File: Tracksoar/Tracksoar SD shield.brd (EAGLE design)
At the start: 44 x 19.5 mm, 8 parts, among them U1 HEX_CONVERTER

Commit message: removed old shields
removed square shields and added values to shield passives
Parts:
- C1: value (none) -> 10uf
- C2: value (none) -> .1uf
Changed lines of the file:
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@@
 <attribute name="PROD_ID" value="IC-09604" x="24.511" y="8.89" size="1.778" layer="28" rot="MR270" display="off"/>
 </element>
-<element name="C1" library="SparkFun-Passives" package="0805" value="" x="26.2636" y="16.891" rot="MR180"/>
-<element name="C2" library="SparkFun-Passives" package="0805" value="" x="26.2382" y="15.1638" rot="MR180"/>
+<element name="C1" library="SparkFun-Passives" package="0805" value="10uf" x="26.2636" y="16.891" rot="MR180"/>
+<element name="C2" library="SparkFun-Passives" package="0805" value=".1uf" x="26.2382" y="15.1638" rot="MR180"/>
 </elements>
 <signals>

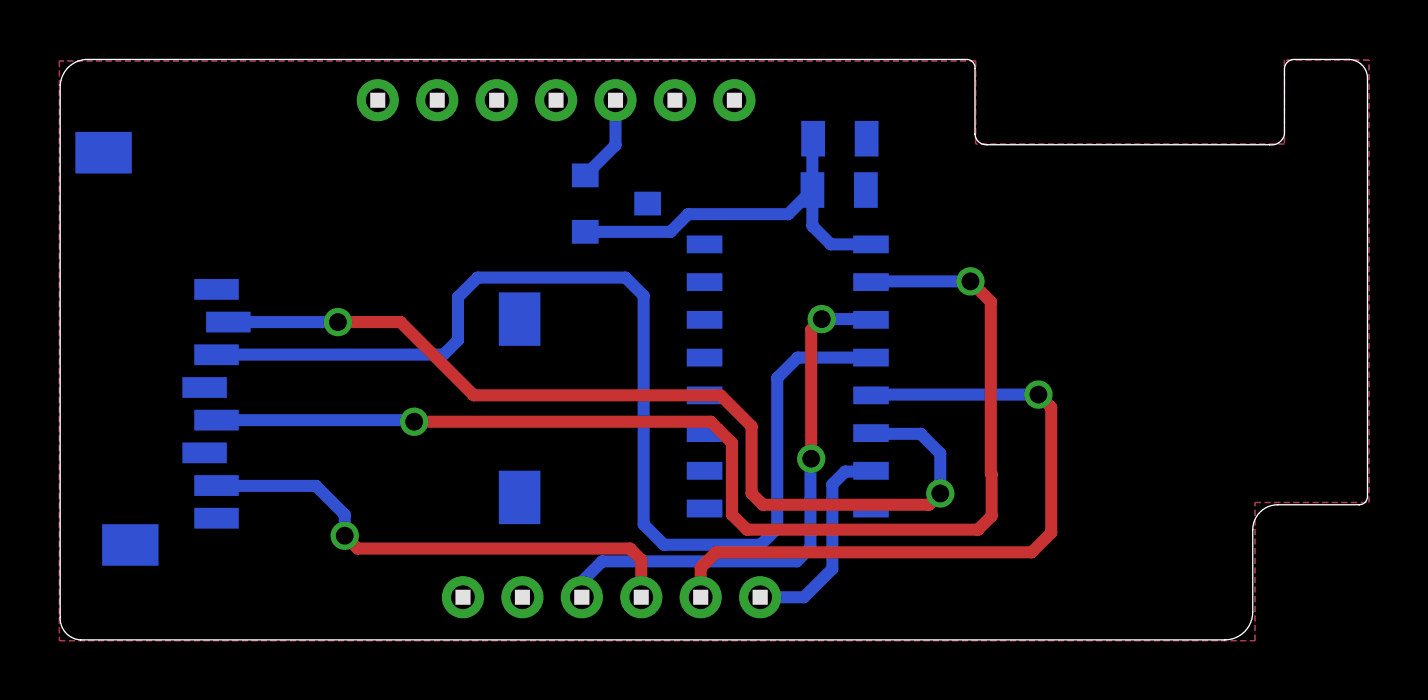
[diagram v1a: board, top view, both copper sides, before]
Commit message: Fixed shield board length
fixed the shield length to not interfere with power and radio
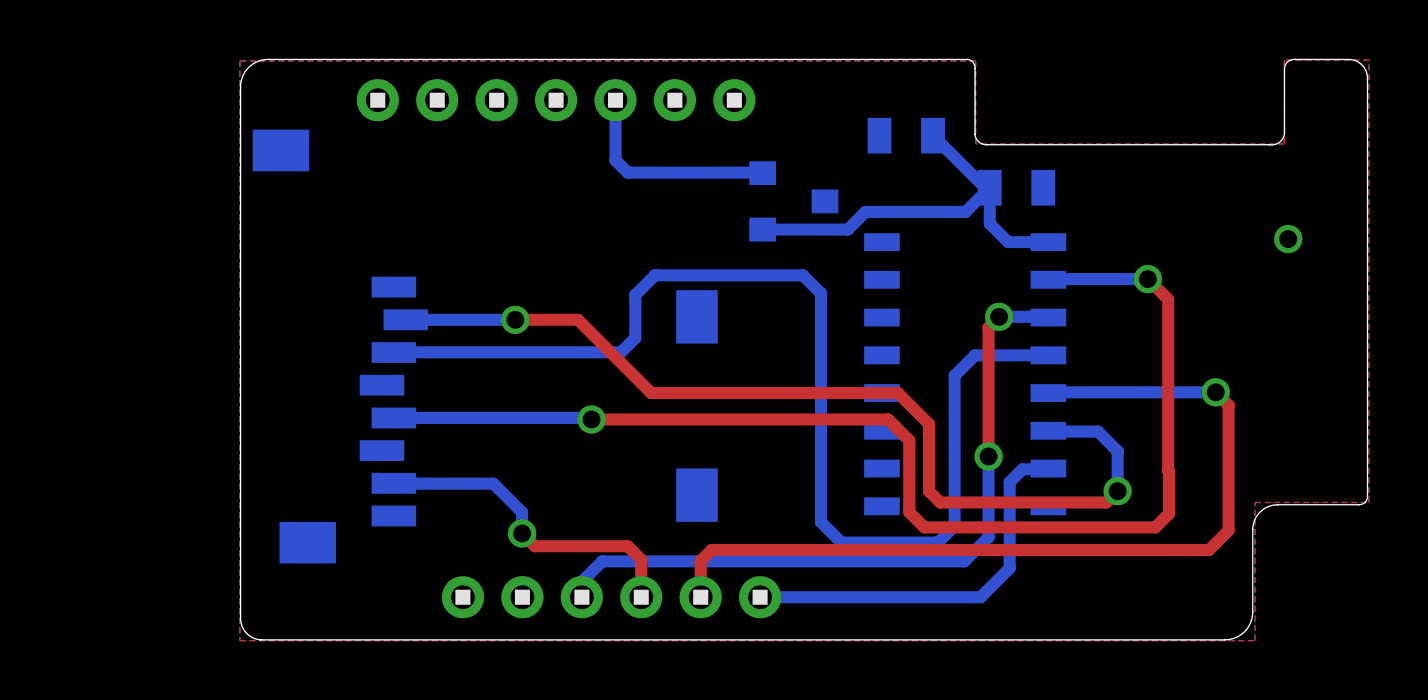
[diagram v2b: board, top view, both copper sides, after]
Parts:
- moved C2 5.97 mm to (32.2, 15.2)
- moved U1 5.97 mm to (30.5, 8.97)
- moved U$1 5.97 mm to (21.9, 2.90)
- moved U$2 5.97 mm to (24.7, 14.8)
- moved C1 2.24 mm to (28.5, 17.0), turned to 0 degrees
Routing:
- net MOSI: track 23.7 -> 29.9 mm
- net SS: track 7.16 -> 13.2 mm
- net MISO: track 17.0 -> 11.1 mm
- net SCK: track 18.2 -> 24.1 mm
- net VCC: track 2.95 -> 7.15 mm
- net 3V: track 13.4 -> 14.3 mm
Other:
- board size 44 x 19.5 mm -> 37.9 x 19.5 mm

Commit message: replaced sd with eeprom
the atmega328p does not have enough SRAM to handle the Trackuino duties
and SD read / write. It has been replace with an ST Micro M24M02 2Mb
eeprom. This will result in much less RAM usage, a smaller BOM, lower
cost, and lower power usage. However it also means we lose portability
of storage and easy computer interfacing. We’ll look at revising this
in future versions.
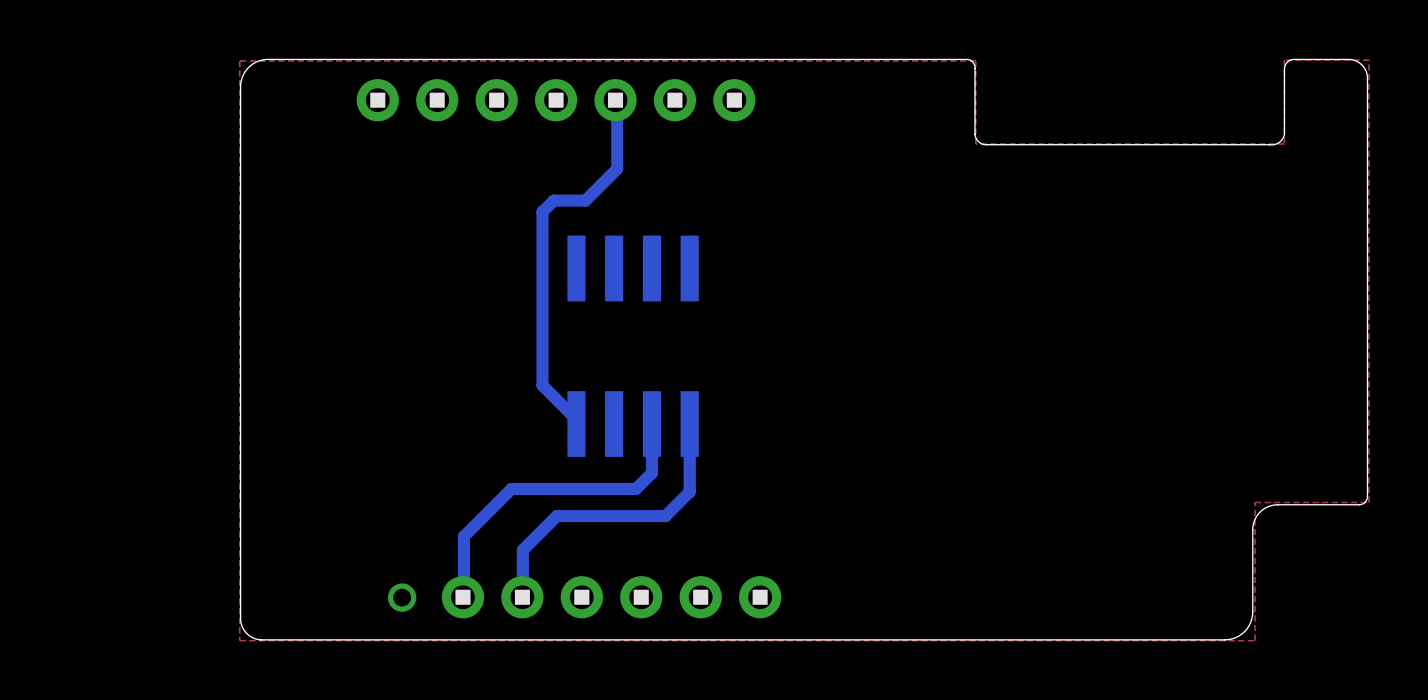
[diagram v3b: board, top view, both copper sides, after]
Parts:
- removed C1: 10uf, SparkFun-Passives:0805
- removed C2: .1uf, SparkFun-Passives:0805
- removed U$1: MICROSD, adafruit:MICROSD
- removed U$2: LM3480IM4, SparkFun-PowerIC:SOT23-3
- U1: value HEX_CONVERTER -> EEPROM-I2CSMD; device SparkFun-DigitalIC:SO016 -> SparkFun-DigitalIC:SO08
- moved U1 11.2 mm to (19.3, 9.91), turned to 180 degrees
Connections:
- removed net 3V: C1.1, C2.1, U$2.1, U1.1
- removed net CS: U$1.2, U1.6
- removed net DI: U$1.3, U1.4
- removed net SCLK: U$1.5, U1.2
- net GND: now also U1.4; no longer C1.2, C2.2, U$1.6, U$1.MT1, U$1.MT2, U$2.3, U1.11, U1.14, U1.8, U1.9
- net MISO: no longer U$1.7
- net MOSI: no longer U1.5
- net SCK: no longer U1.3
- net SCL: now also U1.6
- net SDA: now also U1.5
- net SS: no longer U1.7
- net VCC: now also U1.8; no longer U$2.2
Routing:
- net SCLK: track 40.8 -> 0.00 mm, vias 2 -> 0
- net DI: track 37.8 -> 0.00 mm
- net CS: track 31.9 -> 0.00 mm, vias 2 -> 0
- net MOSI: track 29.9 -> 0.00 mm, vias 1 -> 0
- net SCK: track 24.1 -> 0.00 mm, vias 2 -> 0
- net 3V: track 14.3 -> 0.00 mm
- net SS: track 13.2 -> 0.00 mm
- net MISO: track 11.1 -> 0.00 mm, vias 1 -> 0
- net SCL: track 0.00 -> 10.9 mm
- net SDA: track 0.00 -> 10.3 mm
- net VCC: track 7.15 -> 13.1 mm

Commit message: resolved 1.6.5+ compiling issues
resolved issues in afsk_avr.cpp / h that prevented the firmware from
compiling in 1.6.5+
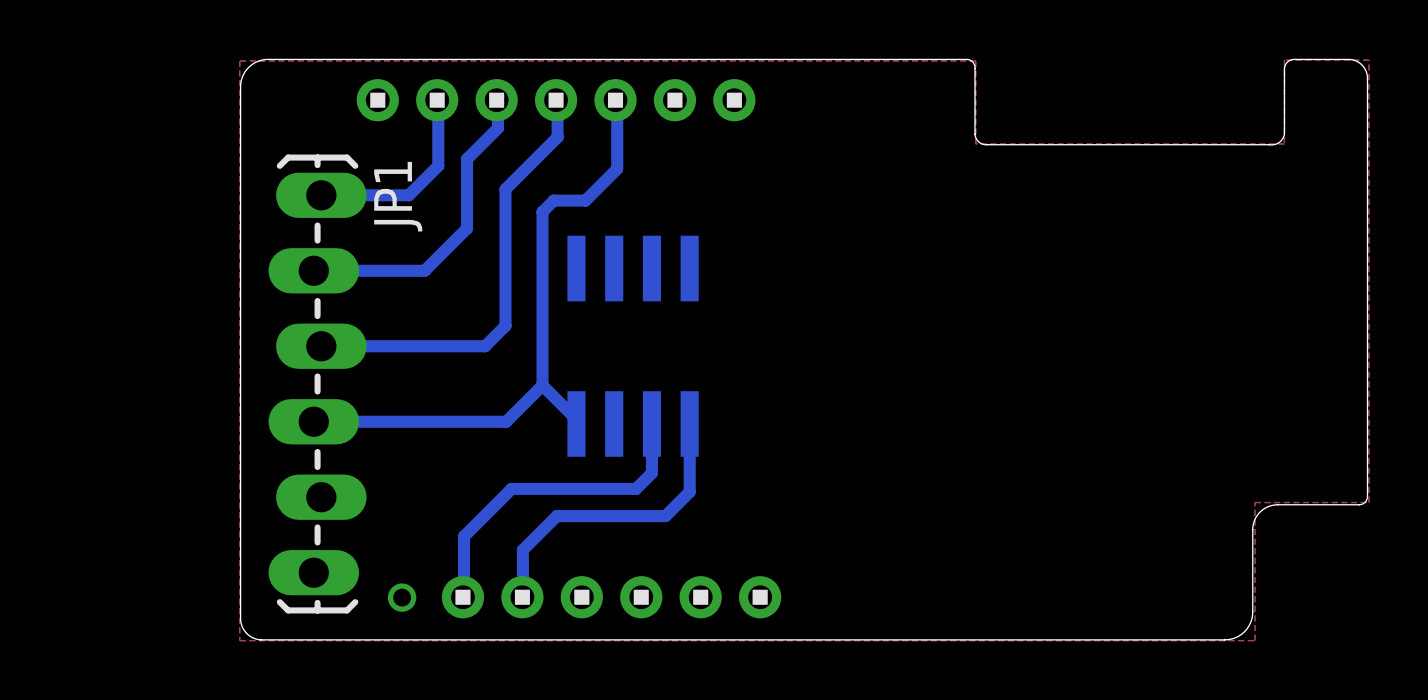
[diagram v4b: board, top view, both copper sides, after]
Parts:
- added JP1: (no value), SparkFun-Connectors:1X06_LOCK_LONGPADS
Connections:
- net DTR: now also JP1.1
- net GND: now also JP1.5, JP1.6
- net RXO: now also JP1.3
- net TXO: now also JP1.2
- net VCC: now also JP1.4
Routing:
- net RXO: track 0.00 -> 14.8 mm
- net TXO: track 0.00 -> 10.5 mm
- net VCC: track 13.1 -> 21.3 mm
- net DTR: track 0.00 -> 6.57 mm
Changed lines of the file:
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@@
 <?xml version="1.0" encoding="utf-8"?>
 <!DOCTYPE eagle SYSTEM "eagle.dtd">
-<eagle version="7.3.0">
+<eagle version="7.5.0">
 <drawing>
 <settings>
@@
 <element name="SPI/I2C" library="headers(2mm)" package="1X6" value="1X6" x="18.58" y="1.46"/>
 <element name="U1" library="SparkFun-DigitalIC" package="SO08" value="EEPROM-I2CSMD" x="19.304" y="9.906" rot="MR180"/>
+<element name="JP1" library="SparkFun-Connectors" package="1X06_LOCK_LONGPADS" value="" x="8.8138" y="14.986" rot="R270"/>
 </elements>
 <signals>
@@
 <contactref element="U1" pad="4"/>
 <via x="11.5316" y="1.4478" extent="1-16" drill="0.6"/>
+<contactref element="JP1" pad="6"/>
+<contactref element="JP1" pad="5"/>
 </signal>
 <signal name="VCC">
@@
 <wire x1="18.7706" y1="15.875" x2="18.7706" y2="18.129" width="0.4064" layer="16"/>
 <wire x1="18.7706" y1="18.129" x2="18.7132" y2="18.1864" width="0.4064" layer="16"/>
+<contactref element="JP1" pad="4"/>
+<wire x1="8.5598" y1="7.366" x2="15.0368" y2="7.366" width="0.4064" layer="16"/>
+<wire x1="15.0368" y1="7.366" x2="16.256" y2="8.5852" width="0.4064" layer="16"/>
 </signal>
 <signal name="DTR">
 <contactref element="FTDI" pad="6"/>
+<contactref element="JP1" pad="1"/>
+<wire x1="8.8138" y1="14.986" x2="11.7602" y2="14.986" width="0.4064" layer="16"/>
+<wire x1="11.7602" y1="14.986" x2="12.7508" y2="15.9766" width="0.4064" layer="16"/>
+<wire x1="12.7508" y1="15.9766" x2="12.7508" y2="18.1488" width="0.4064" layer="16"/>
+<wire x1="12.7508" y1="18.1488" x2="12.7132" y2="18.1864" width="0.4064" layer="16"/>
 </signal>
 <signal name="RXO">
 <contactref element="FTDI" pad="4"/>
+<contactref element="JP1" pad="3"/>
+<wire x1="8.8138" y1="9.906" x2="14.3256" y2="9.906" width="0.4064" layer="16"/>
+<wire x1="14.3256" y1="9.906" x2="15.0114" y2="10.5918" width="0.4064" layer="16"/>
+<wire x1="15.0114" y1="10.5918" x2="15.0114" y2="15.1892" width="0.4064" layer="16"/>
+<wire x1="15.0114" y1="15.1892" x2="16.764" y2="16.9418" width="0.4064" layer="16"/>
+<wire x1="16.764" y1="16.9418" x2="16.764" y2="18.1356" width="0.4064" layer="16"/>
+<wire x1="16.764" y1="18.1356" x2="16.7132" y2="18.1864" width="0.4064" layer="16"/>
 </signal>
 <signal name="TXO">
 <contactref element="FTDI" pad="5"/>
+<contactref element="JP1" pad="2"/>
+<wire x1="8.5598" y1="12.446" x2="12.2936" y2="12.446" width="0.4064" layer="16"/>
+<wire x1="12.2936" y1="12.446" x2="13.716" y2="13.8684" width="0.4064" layer="16"/>
+<wire x1="13.716" y1="13.8684" x2="13.716" y2="16.2052" width="0.4064" layer="16"/>
+<wire x1="13.716" y1="16.2052" x2="14.7574" y2="17.2466" width="0.4064" layer="16"/>
+<wire x1="14.7574" y1="17.2466" x2="14.7574" y2="18.1422" width="0.4064" layer="16"/>
+<wire x1="14.7574" y1="18.1422" x2="14.7132" y2="18.1864" width="0.4064" layer="16"/>
 </signal>
 <signal name="MISO">

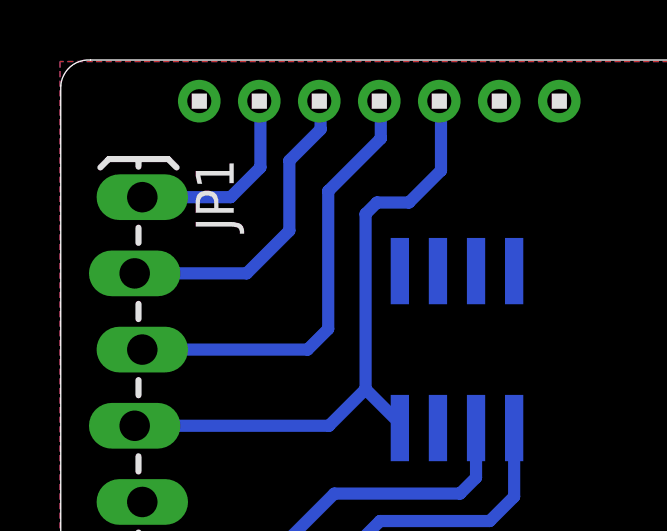
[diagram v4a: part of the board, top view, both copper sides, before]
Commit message: added eeprom silkscreen
added silkscreen markings to the EEPROM FTDI connector
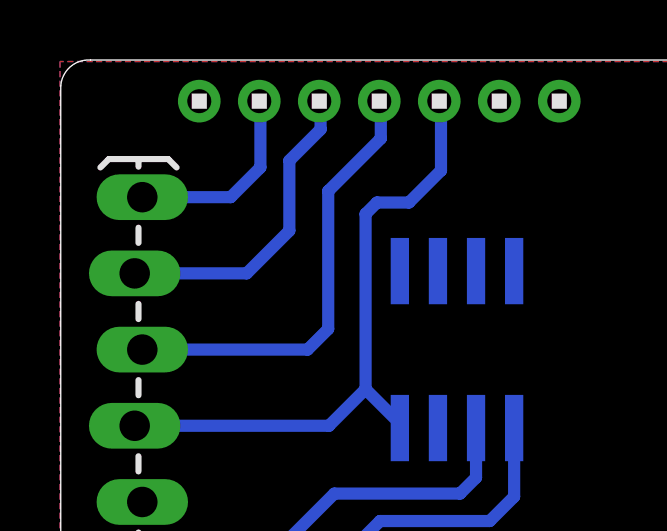
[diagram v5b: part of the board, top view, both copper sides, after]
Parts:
- renumbered JP1 to FTDI-1
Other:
- board text added: "5v"
- board text added: "RESET"
- board text added: "RX"
- board text added: "TX"
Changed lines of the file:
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@@
 <?xml version="1.0" encoding="utf-8"?>
 <!DOCTYPE eagle SYSTEM "eagle.dtd">
-<eagle version="7.5.0">
+<eagle version="7.3.0">
 <drawing>
 <settings>
@@
 <wire x1="40.9956" y1="4.572" x2="43.7388" y2="4.572" width="0" layer="20"/>
 <wire x1="43.7388" y1="4.572" x2="44.0182" y2="4.8514" width="0" layer="20" curve="90"/>
+<text x="12.1158" y="5.4864" size="1.016" layer="26" rot="MR270">GND</text>
+<text x="12.7762" y="6.985" size="1.016" layer="26" rot="MR0">5v</text>
+<text x="15.4686" y="14.3764" size="1.016" layer="26" rot="MR0">RESET</text>
+<text x="12.9032" y="11.7856" size="1.016" layer="26" rot="MR0">TX</text>
+<text x="12.9286" y="9.3472" size="1.016" layer="26" rot="MR0">RX</text>
 </plain>
 <attributes>
@@
 <element name="SPI/I2C" library="headers(2mm)" package="1X6" value="1X6" x="18.58" y="1.46"/>
 <element name="U1" library="SparkFun-DigitalIC" package="SO08" value="EEPROM-I2CSMD" x="19.304" y="9.906" rot="MR180"/>
-<element name="JP1" library="SparkFun-Connectors" package="1X06_LOCK_LONGPADS" value="" x="8.8138" y="14.986" rot="R270"/>
+<element name="FTDI-1" library="SparkFun-Connectors" package="1X06_LOCK_LONGPADS" value="" x="8.8138" y="14.986" smashed="yes" rot="R270">
+<attribute name="VALUE" x="5.5118" y="16.256" size="1.27" layer="27" font="vector" rot="R270"/>
+</element>
 </elements>
 <signals>
@@
 <contactref element="U1" pad="4"/>
 <via x="11.5316" y="1.4478" extent="1-16" drill="0.6"/>
-<contactref element="JP1" pad="6"/>
-<contactref element="JP1" pad="5"/>
+<contactref element="FTDI-1" pad="6"/>
+<contactref element="FTDI-1" pad="5"/>
 </signal>
 <signal name="VCC">
@@
 <wire x1="18.7706" y1="15.875" x2="18.7706" y2="18.129" width="0.4064" layer="16"/>
 <wire x1="18.7706" y1="18.129" x2="18.7132" y2="18.1864" width="0.4064" layer="16"/>
-<contactref element="JP1" pad="4"/>
+<contactref element="FTDI-1" pad="4"/>
 <wire x1="8.5598" y1="7.366" x2="15.0368" y2="7.366" width="0.4064" layer="16"/>
 <wire x1="15.0368" y1="7.366" x2="16.256" y2="8.5852" width="0.4064" layer="16"/>
@@
 <signal name="DTR">
 <contactref element="FTDI" pad="6"/>
-<contactref element="JP1" pad="1"/>
+<contactref element="FTDI-1" pad="1"/>
 <wire x1="8.8138" y1="14.986" x2="11.7602" y2="14.986" width="0.4064" layer="16"/>
 <wire x1="11.7602" y1="14.986" x2="12.7508" y2="15.9766" width="0.4064" layer="16"/>
@@
 <signal name="RXO">
 <contactref element="FTDI" pad="4"/>
-<contactref element="JP1" pad="3"/>
+<contactref element="FTDI-1" pad="3"/>
 <wire x1="8.8138" y1="9.906" x2="14.3256" y2="9.906" width="0.4064" layer="16"/>
 <wire x1="14.3256" y1="9.906" x2="15.0114" y2="10.5918" width="0.4064" layer="16"/>
@@
 <signal name="TXO">
 <contactref element="FTDI" pad="5"/>
-<contactref element="JP1" pad="2"/>
+<contactref element="FTDI-1" pad="2"/>
 <wire x1="8.5598" y1="12.446" x2="12.2936" y2="12.446" width="0.4064" layer="16"/>
 <wire x1="12.2936" y1="12.446" x2="13.716" y2="13.8684" width="0.4064" layer="16"/>
